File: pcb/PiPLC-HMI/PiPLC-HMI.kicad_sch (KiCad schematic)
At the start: 22 parts, among them J1 Conn_02x12_Odd_Even, J2 KNX, J3 Wago Pin Header 1mm, J4 Wago Pin Header 1mm

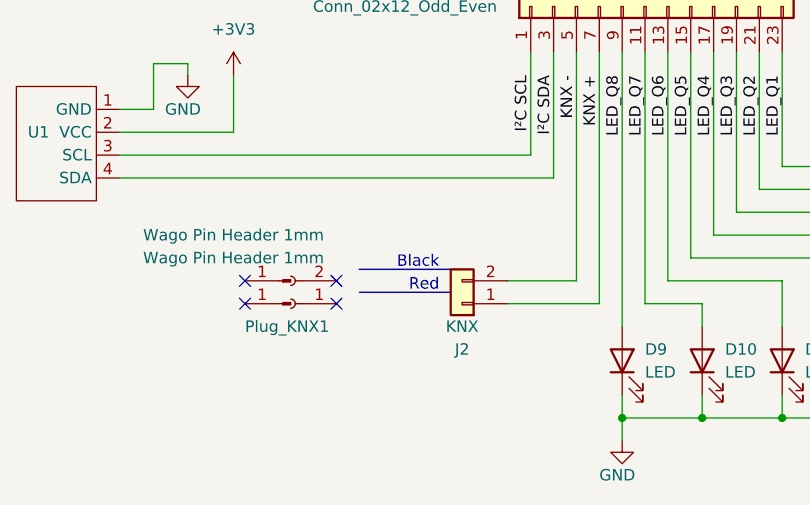
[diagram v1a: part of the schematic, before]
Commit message: [HMI] Schematic Beautification
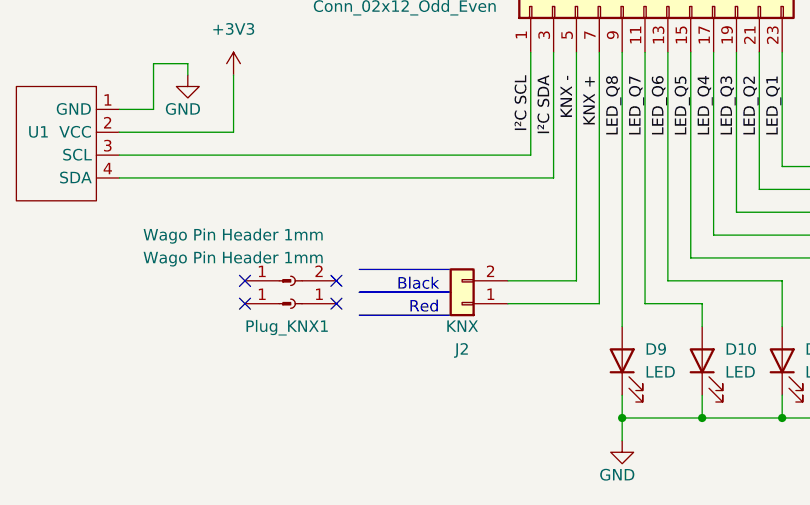
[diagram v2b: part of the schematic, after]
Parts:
- D1, D10, D11, D12, D13, D14, D15, D16, D2, D3, D4, D5, D6, D7, D8, D9: LCSC (none) -> C417347
- J1: LCSC (none) -> C2894973
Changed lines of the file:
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@@
   (no_connect (at 118.11 125.73))
   (no_connect (at 107.95 123.19))
-  (wire (pts (xy 176.53 120.65) (xy 157.48 120.65))
-    (stroke (width 0) (type default))
-  )
   (polyline (pts (xy 130.81 121.92) (xy 120.65 121.92))
     (stroke (width 0) (type solid))
   )
-  (wire (pts (xy 149.86 135.89) (xy 149.86 138.43))
-    (stroke (width 0) (type default))
-  )
-  (wire (pts (xy 149.86 43.18) (xy 149.86 45.72))
+  (wire (pts (xy 176.53 120.65) (xy 157.48 120.65))
     (stroke (width 0) (type default))
   )
@@
     (stroke (width 0) (type solid))
   )
+  (wire (pts (xy 149.86 135.89) (xy 149.86 138.43))
+    (stroke (width 0) (type default))
+  )
+  (wire (pts (xy 149.86 43.18) (xy 149.86 45.72))
+    (stroke (width 0) (type default))
+  )
+  (polyline (pts (xy 130.81 127) (xy 120.65 127))
+    (stroke (width 0) (type solid))
+  )
   (wire (pts (xy 93.98 111.76) (xy 142.24 111.76))
     (stroke (width 0) (type default))
@@
     (stroke (width 0) (type default))
   )
-  (polyline (pts (xy 130.81 121.92) (xy 120.65 121.92))
+  (polyline (pts (xy 130.81 124.46) (xy 120.65 124.46))
     (stroke (width 0) (type solid))
   )
@@
     (stroke (width 0) (type default))
   )
-  (text "Black" (at 129.54 121.92 0)
+  (text "Black" (at 129.54 124.46 0)
     (effects (font (size 1.27 1.27)) (justify right bottom))
   )
@@
     (effects (font (size 2.5 2.5)) (justify left bottom))
   )
-  (text "Red" (at 129.54 124.46 0)
+  (text "Red" (at 129.54 127 0)
     (effects (font (size 1.27 1.27)) (justify right bottom))
   )
@@
     )
     (property "Datasheet" "~" (at 149.86 49.53 0)
+      (effects (font (size 1.27 1.27)) hide)
+    )
+    (property "LCSC" "C417347" (at 149.86 49.53 0)
       (effects (font (size 1.27 1.27)) hide)
     )
@@
       (effects (font (size 1.27 1.27)) hide)
     )
+    (property "LCSC" "C417347" (at 212.09 49.53 0)
+      (effects (font (size 1.27 1.27)) hide)
+    )
     (pin "1")
     (pin "2")
@@
       (effects (font (size 1.27 1.27)) hide)
     )
+    (property "LCSC" "C417347" (at 158.75 132.08 0)
+      (effects (font (size 1.27 1.27)) hide)
+    )
     (pin "1")
     (pin "2")
@@
     )
     (property "Datasheet" "~" (at 152.4 92.71 0)
+      (effects (font (size 1.27 1.27)) hide)
+    )
+    (property "LCSC" "C2894973" (at 152.4 92.71 90)
       (effects (font (size 1.27 1.27)) hide)
     )
@@
       (effects (font (size 1.27 1.27)) hide)
     )
+    (property "LCSC" "C417347" (at 212.09 132.08 0)
+      (effects (font (size 1.27 1.27)) hide)
+    )
     (pin "1")
     (pin "2")
@@
     )
     (property "Datasheet" "~" (at 149.86 132.08 0)
+      (effects (font (size 1.27 1.27)) hide)
+    )
+    (property "LCSC" "C417347" (at 149.86 132.08 0)
       (effects (font (size 1.27 1.27)) hide)
     )
@@
       (effects (font (size 1.27 1.27)) hide)
     )
+    (property "LCSC" "C417347" (at 167.64 132.08 0)
+      (effects (font (size 1.27 1.27)) hide)
+    )
     (pin "1")
     (pin "2")
@@
     )
     (property "Datasheet" "~" (at 176.53 49.53 0)
+      (effects (font (size 1.27 1.27)) hide)
+    )
+    (property "LCSC" "C417347" (at 176.53 49.53 0)
       (effects (font (size 1.27 1.27)) hide)
     )
@@
       (effects (font (size 1.27 1.27)) hide)
     )
+    (property "LCSC" "C417347" (at 167.64 49.53 0)
+      (effects (font (size 1.27 1.27)) hide)
+    )
     (pin "1")
     (pin "2")
@@
     )
     (property "Datasheet" "~" (at 203.2 132.08 0)
+      (effects (font (size 1.27 1.27)) hide)
+    )
+    (property "LCSC" "C417347" (at 203.2 132.08 0)
       (effects (font (size 1.27 1.27)) hide)
     )
@@
       (effects (font (size 1.27 1.27)) hide)
     )
+    (property "LCSC" "C417347" (at 185.42 49.53 0)
+      (effects (font (size 1.27 1.27)) hide)
+    )
     (pin "1")
     (pin "2")
@@
       (effects (font (size 1.27 1.27)) hide)
     )
+    (property "LCSC" "C417347" (at 158.75 49.53 0)
+      (effects (font (size 1.27 1.27)) hide)
+    )
     (pin "1")
     (pin "2")
@@
       (effects (font (size 1.27 1.27)) hide)
     )
+    (property "LCSC" "C417347" (at 185.42 132.08 0)
+      (effects (font (size 1.27 1.27)) hide)
+    )
     (pin "1")
     (pin "2")
@@
       (effects (font (size 1.27 1.27)) hide)
     )
+    (property "LCSC" "C417347" (at 176.53 132.08 0)
+      (effects (font (size 1.27 1.27)) hide)
+    )
     (pin "1")
     (pin "2")
@@
       (effects (font (size 1.27 1.27)) hide)
     )
+    (property "LCSC" "C417347" (at 203.2 49.53 0)
+      (effects (font (size 1.27 1.27)) hide)
+    )
     (pin "1")
     (pin "2")
@@
       (effects (font (size 1.27 1.27)) hide)
     )
+    (property "LCSC" "C417347" (at 194.31 132.08 0)
+      (effects (font (size 1.27 1.27)) hide)
+    )
     (pin "1")
     (pin "2")
@@
       (effects (font (size 1.27 1.27)) hide)
     )
+    (property "LCSC" "C417347" (at 194.31 49.53 0)
+      (effects (font (size 1.27 1.27)) hide)
+    )

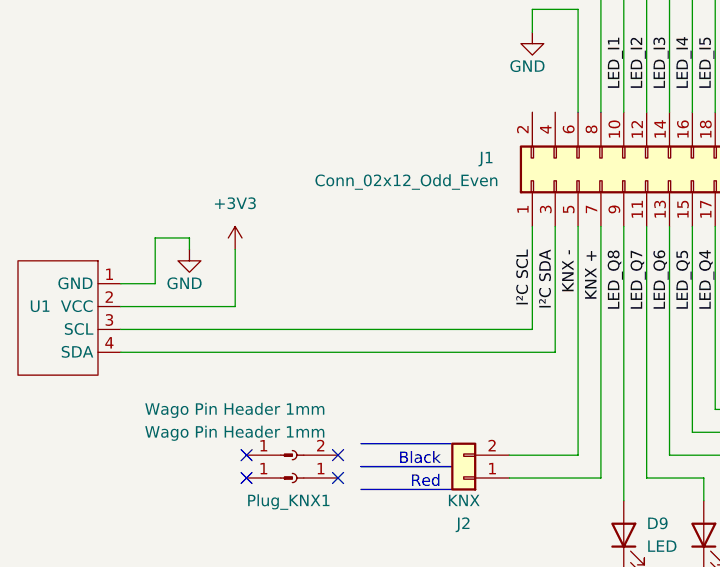
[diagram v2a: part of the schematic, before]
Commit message: [Mainboard][HMI] Remove display
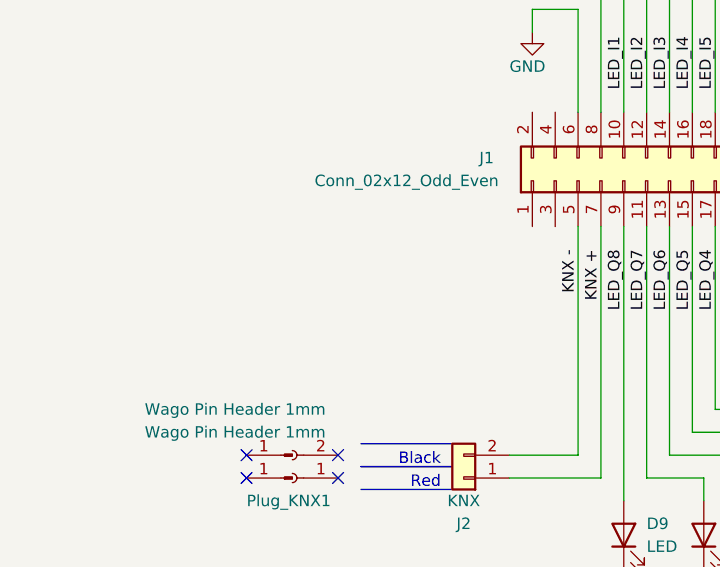
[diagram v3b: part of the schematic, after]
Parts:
- removed U1: ~, MeineBib:HS96L03, symbol MeineBib:HS96L03
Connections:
- net I²C SCL: no longer names the net of J1.1 (Pin_1)
- net I²C SDA: no longer names the net of J1.3 (Pin_3)
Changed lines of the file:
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@@
     (stroke (width 0) (type solid))
   )
-  (wire (pts (xy 93.98 111.76) (xy 142.24 111.76))
-    (stroke (width 0) (type default))
-  )
   (wire (pts (xy 147.32 97.79) (xy 147.32 125.73))
     (stroke (width 0) (type default))
   )
-  (wire (pts (xy 106.68 106.68) (xy 93.98 106.68))
-    (stroke (width 0) (type default))
-  )
   (wire (pts (xy 147.32 125.73) (xy 137.16 125.73))
     (stroke (width 0) (type default))
@@
     (stroke (width 0) (type default))
   )
-  (wire (pts (xy 97.79 104.14) (xy 97.79 99.06))
-    (stroke (width 0) (type default))
-  )
   (wire (pts (xy 147.32 43.18) (xy 149.86 43.18))
     (stroke (width 0) (type default))
@@
     (stroke (width 0) (type default))
   )
-  (wire (pts (xy 101.6 99.06) (xy 101.6 100.33))
-    (stroke (width 0) (type default))
-  )
   (wire (pts (xy 176.53 62.23) (xy 176.53 53.34))
     (stroke (width 0) (type default))
@@
     (stroke (width 0) (type default))
   )
-  (wire (pts (xy 93.98 104.14) (xy 97.79 104.14))
-    (stroke (width 0) (type default))
-  )
   (wire (pts (xy 203.2 69.85) (xy 203.2 53.34))
     (stroke (width 0) (type default))
@@
     (stroke (width 0) (type default))
   )
-  (wire (pts (xy 139.7 97.79) (xy 139.7 109.22))
-    (stroke (width 0) (type default))
-  )
   (wire (pts (xy 158.75 128.27) (xy 158.75 125.73))
     (stroke (width 0) (type default))
@@
   )
   (wire (pts (xy 176.53 43.18) (xy 176.53 45.72))
-    (stroke (width 0) (type default))
-  )
-  (wire (pts (xy 142.24 97.79) (xy 142.24 111.76))
     (stroke (width 0) (type default))
   )
@@
     (stroke (width 0) (type default))
   )
-  (wire (pts (xy 106.68 100.33) (xy 106.68 106.68))
-    (stroke (width 0) (type default))
-  )
   (wire (pts (xy 152.4 125.73) (xy 152.4 97.79))
     (stroke (width 0) (type default))
@@
     (stroke (width 0) (type default))
   )
-  (wire (pts (xy 97.79 99.06) (xy 101.6 99.06))
-    (stroke (width 0) (type default))
-  )
   (wire (pts (xy 137.16 123.19) (xy 144.78 123.19))
     (stroke (width 0) (type default))
@@
   )
   (wire (pts (xy 176.53 138.43) (xy 167.64 138.43))
-    (stroke (width 0) (type default))
-  )
-  (wire (pts (xy 139.7 109.22) (xy 93.98 109.22))
     (stroke (width 0) (type default))
   )
@@
     (effects (font (size 1.27 1.27)) (justify right bottom))
   )
-  (label "I²C SDA" (at 142.24 100.33 270) (fields_autoplaced)
-    (effects (font (size 1.27 1.27)) (justify right bottom))
-  )
-  (label "I²C SCL" (at 139.7 100.33 270) (fields_autoplaced)
-    (effects (font (size 1.27 1.27)) (justify right bottom))
-  )
   (label "LED_Q1" (at 167.64 100.33 270) (fields_autoplaced)
     (effects (font (size 1.27 1.27)) (justify right bottom))
@@
         (path "/8e79ca85-0324-46f6-b833-7804912a961b"
           (reference "D8") (unit 1)
-        )
-      )
-    )
-  )
-  (symbol (lib_id "MeineBib:HS96L03") (at 88.9 107.95 270) (unit 1)
-    (in_bom yes) (on_board yes) (dnp no)
-    (property "Reference" "U1" (at 83.82 106.68 90)
-      (effects (font (size 1.27 1.27)) (justify left))
-    )
-    (property "Value" "~" (at 88.9 107.95 0)
-      (effects (font (size 1.27 1.27)))
-    )
-    (property "Footprint" "MeineBib:HS96L03" (at 88.9 107.95 0)
-      (effects (font (size 1.27 1.27)) hide)
-    )
-    (property "Datasheet" "https://datasheet.lcsc.com/lcsc/2306271450_HS-HS96L03W2C03_C5248080.pdf" (at 88.9 107.95 0)
-      (effects (font (size 1.27 1.27)) hide)
-    )
-    (property "LCSC" "C5248080" (at 88.9 107.95 0)
-      (effects (font (size 1.27 1.27)) hide)
-    )
-    (pin "1")
-    (pin "2")
-    (pin "3")
-    (pin "4")
-    (instances
-      (project "PiPLC-HMI"
-        (path "/8e79ca85-0324-46f6-b833-7804912a961b"
-          (reference "U1") (unit 1)
         )
       )
@@
         )
       )
-    )
-  )
-  (symbol (lib_id "power:GND") (at 101.6 100.33 0) (unit 1)
-    (in_bom yes) (on_board yes) (dnp no)
-    (property "Reference" "#PWR04" (at 101.6 106.68 0)
-      (effects (font (size 1.27 1.27)) hide)
-    )
-    (property "Value" "GND" (at 99.06 104.14 0)
-      (effects (font (size 1.27 1.27)) (justify left))
-    )
-    (property "Footprint" "" (at 101.6 100.33 0)
-      (effects (font (size 1.27 1.27)) hide)
-    )
-    (property "Datasheet" "" (at 101.6 100.33 0)
-      (effects (font (size 1.27 1.27)) hide)
-    )
-    (pin "1")
-    (instances
-      (project "PiPLC-HMI"
-        (path "/8e79ca85-0324-46f6-b833-7804912a961b"
-          (reference "#PWR04") (unit 1)
-        )
-      )
-      (project "PiPLC-Base"
-        (path "/93ebf745-625a-4d9e-8f47-45e91f30ef94"
-          (reference "#PWR045") (unit 1)
-        )
-      )
-    )
-  )
-  (symbol (lib_id "power:+3V3") (at 106.68 100.33 0) (unit 1)
-    (in_bom yes) (on_board yes) (dnp no) (fields_autoplaced)
-    (property "Reference" "#PWR05" (at 106.68 104.14 0)
-      (effects (font (size 1.27 1.27)) hide)
-    )
-    (property "Value" "+3V3" (at 106.68 95.25 0)
-      (effects (font (size 1.27 1.27)))
-    )
-    (property "Footprint" "" (at 106.68 100.33 0)
-      (effects (font (size 1.27 1.27)) hide)
-    )
-    (property "Datasheet" "" (at 106.68 100.33 0)
-      (effects (font (size 1.27 1.27)) hide)
-    )
-    (pin "1")
-    (instances
-      (project "PiPLC-HMI"
-        (path "/8e79ca85-0324-46f6-b833-7804912a961b"
-          (reference "#PWR05") (unit 1)
-        )
-      )
-      (project "PiPLC-Base"
-        (path "/93ebf745-625a-4d9e-8f47-45e91f30ef94"
-          (reference "#PWR046") (unit 1)
-        )
-      )

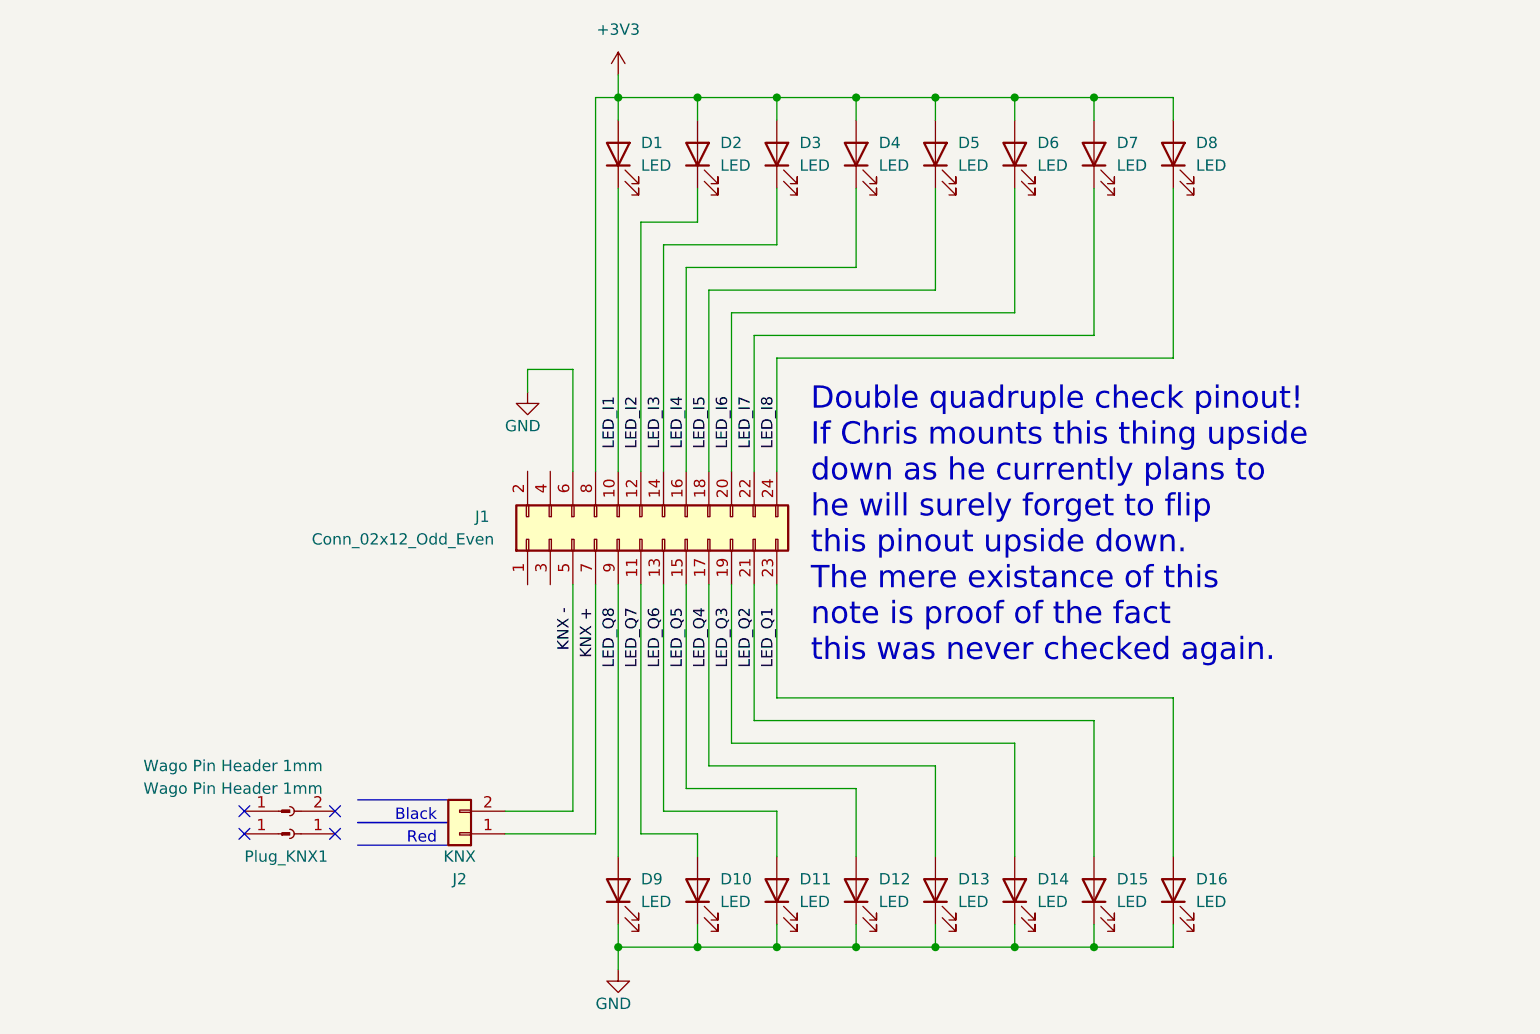
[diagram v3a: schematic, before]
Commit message: Add "5V OK" and "24V OK" LEDs to HMI
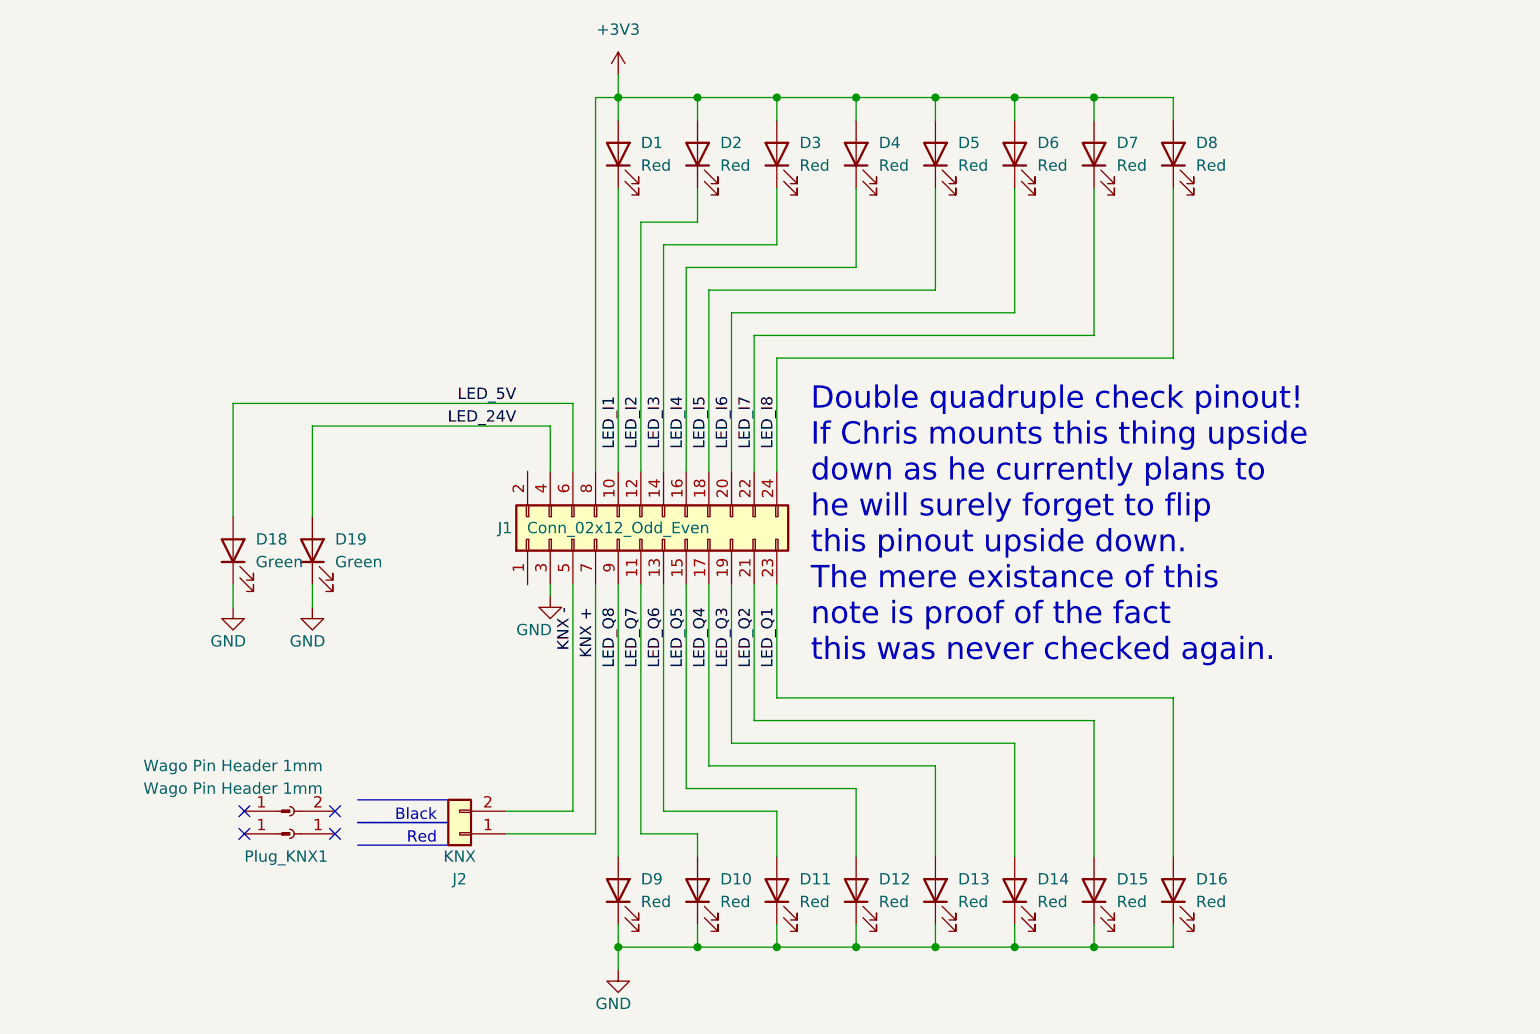
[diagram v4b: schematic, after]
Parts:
- added D18, D19: Green, LED_THT:LED_D5.0mm, symbol Device:LED
- D1, D10, D11, D12, D13, D14, D15, D16, D2, D3, D4, D5, D6, D7, D8, D9: value LED -> Red
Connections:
- net GND: now also J1.3 (Pin_3), D18.1 (K), D19.1 (K); no longer J1.6 (Pin_6)
- net LED_24V: now reaches J1.4 (Pin_4)
- net LED_24V: now also D19.2 (A)
- new net LED_5V: D18.2 (A), J1.6 (Pin_6)

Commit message: [HMI] Add LCSC part number for 1mm pins
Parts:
- J3, J4: LCSC (none) -> C265321
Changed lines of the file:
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@@
       (effects (font (size 1.27 1.27)) hide)
     )
-    (property "LCSC" "~" (at 113.03 123.19 0)
+    (property "LCSC" "C265321" (at 113.03 123.19 0)
       (effects (font (size 1.27 1.27)) hide)
     )
@@
       (effects (font (size 1.27 1.27)) hide)
     )
-    (property "LCSC" "~" (at 113.03 125.73 0)
+    (property "LCSC" "C265321" (at 113.03 125.73 0)
       (effects (font (size 1.27 1.27)) hide)
     )

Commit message: [Main][HMI]Minor schematic beautification
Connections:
- no-connect marks 4 -> 6
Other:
- note removed: "Double quadruple check pinout! If Chris mounts this thing upside down as he currently plans to he will surely forget to flip this pinout upside down. The mere existance of this note is proof of the fact this was never checked again."
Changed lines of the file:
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@@
   (junction (at 158.75 138.43) (diameter 0) (color 0 0 0 0)
   )
+  (no_connect (at 139.7 85.09))
   (no_connect (at 107.95 125.73))
   (no_connect (at 118.11 123.19))
   (no_connect (at 118.11 125.73))
   (no_connect (at 107.95 123.19))
+  (no_connect (at 139.7 97.79))
   (polyline (pts (xy 130.81 121.92) (xy 120.65 121.92))
     (stroke (width 0) (type solid))
@@
     (effects (font (size 1.27 1.27)) (justify right bottom))
   )
-  (text "Double quadruple check pinout!\nIf Chris mounts this thing upside\ndown as he currently plans to\nhe will surely forget to flip\nthis pinout upside down.\nThe mere existance of this\nnote is proof of the fact\nthis was never checked again."
-    (at 171.45 106.68 0)
-    (effects (font (size 2.5 2.5)) (justify left bottom))
-  )
   (text "Red" (at 129.54 127 0)
